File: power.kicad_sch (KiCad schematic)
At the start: 37 parts, among them J2 USB_C_Receptacle_USB2.0, Q1 AO3401A, Q2 AO3400A, SW1 SW_SPDT, U2 XC6220B331MR, U3 TLV70237_SOT23-5, U4 LN4913, U5 SRV05-4

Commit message: routed
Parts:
- removed C1: 0.1uF, Capacitor_SMD:C_0603_1608Metric, symbol Device:C
- removed JP3: SolderJumper_3_Open, Jumper:SolderJumper-3_P1.3mm_Open_RoundedPad1.0x1.5mm, symbol Jumper:SolderJumper_3_Open
- removed Q1: AO3401A, Package_TO_SOT_SMD:SOT-23, symbol Transistor_FET:AO3401A
- removed Q2: AO3400A, Package_TO_SOT_SMD:SOT-23, symbol Transistor_FET:AO3400A
- removed R23: 10M, Resistor_SMD:R_0603_1608Metric, symbol Device:R
- removed R9: 1M, Resistor_SMD:R_0603_1608Metric, symbol Device:R
- removed SC?: Solar_Cell, misc:KXOB25-05X3F, symbol Device:Solar_Cell
- removed SW1: SW_SPDT, Button_Switch_SMD:SW_SPDT_PCM12, symbol Switch:SW_SPDT
- removed U4: LN4913, Package_TO_SOT_SMD:SOT-23, symbol Sensor_Magnetic:A1101ELHL
- gave numbers to parts that had none: 19
- renumbered D1 to D3, R8 to R10, R3 to R11, R5 to R12, R7 to R9, U2 to U4, U3 to U5, U5 to U6
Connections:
- net 3V3_EN is gone; now on net SOLAR_OUT: U4.3 (CE)
- net D+: now also U6.1 (IO1), U6.6 (IO4); no longer U6.3 (IO2), U6.4 (IO3)
- net D-: now also U6.3 (IO2), U6.4 (IO3); no longer U6.1 (IO1), U6.6 (IO4)

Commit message: no screen
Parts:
- removed JP3: ~, Jumper:SolderJumper-2_P1.3mm_Open_RoundedPad1.0x1.5mm, symbol Jumper:SolderJumper_2_Open
- removed JP4: SolderJumper_2_Open, Jumper:SolderJumper-2_P1.3mm_Open_RoundedPad1.0x1.5mm, symbol Jumper:SolderJumper_2_Open
- added R7: 1M, Resistor_SMD:R_0603_1608Metric, symbol Device:R_Small
- C4: footprint Capacitor_THT:CP_Radial_D13.0mm_P5.00mm -> Capacitor_THT:CP_Radial_D16.0mm_P7.50mm
- C8: value 47uF -> 4.7uF
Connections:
- net SOLAR_OUT: now also R7.2; no longer U4.3 (CE)
- net at U7.11 (VBAT_OK): now also U4.3 (CE), R7.1
- no-connect marks 4 -> 3
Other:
- moved on the sheet: U4

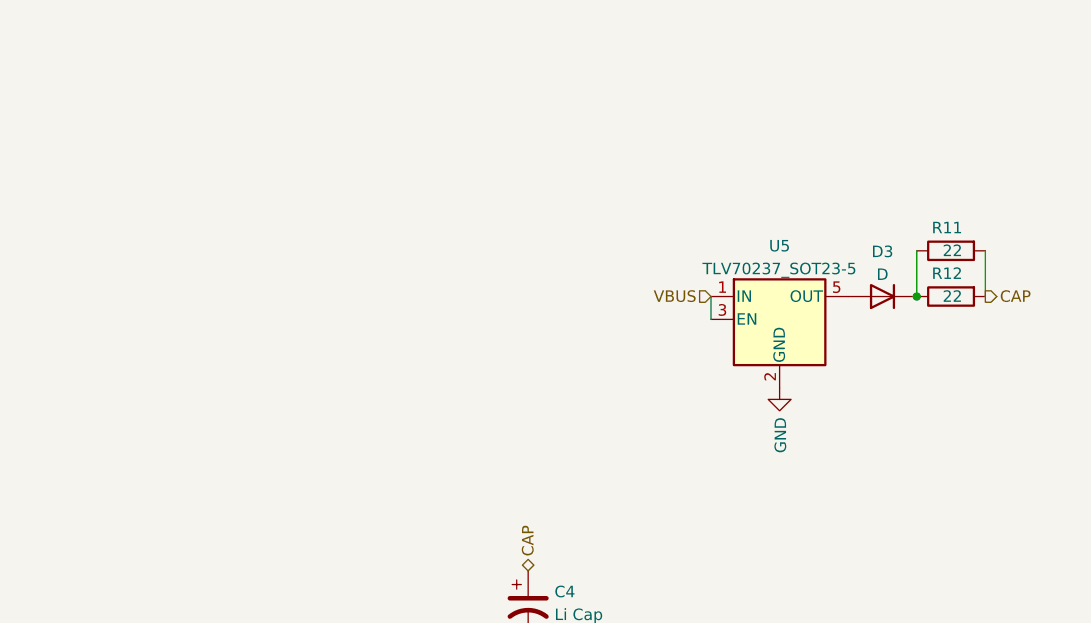
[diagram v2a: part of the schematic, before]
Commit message: scroll wheel + constant current charger
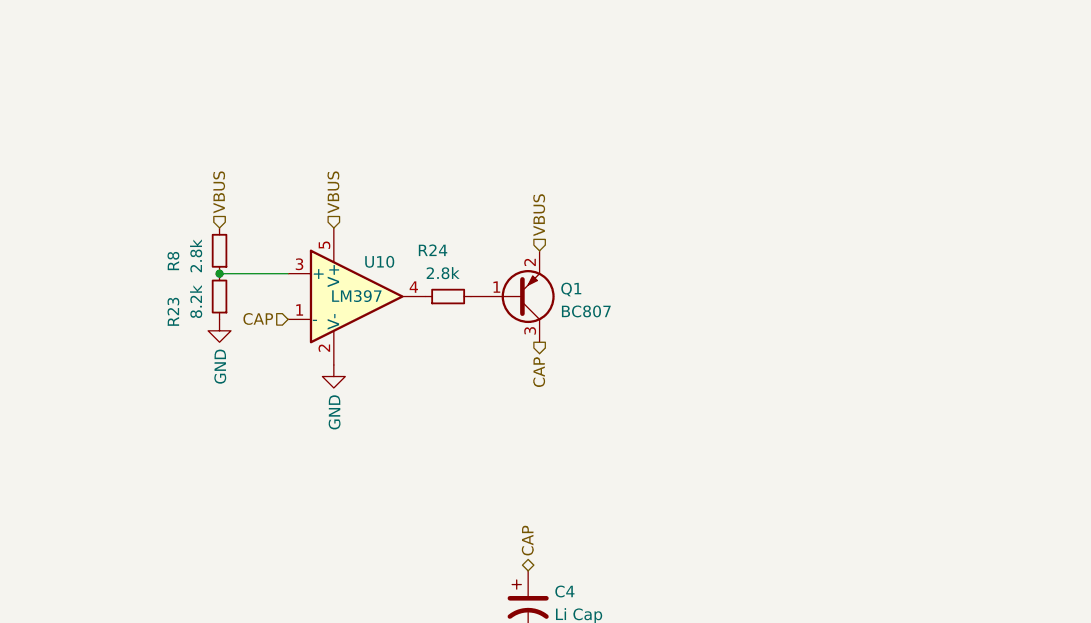
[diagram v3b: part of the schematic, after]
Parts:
- removed D3: D, Diode_SMD:D_SOD-123, symbol Device:D
- removed R11, R12: 22, Resistor_SMD:R_0603_1608Metric, symbol Device:R
- removed U5: TLV70237_SOT23-5, Package_TO_SOT_SMD:SOT-23-5, symbol Regulator_Linear:TLV70237_SOT23-5
- added Q1: BC807, Package_TO_SOT_SMD:SOT-23, symbol Transistor_BJT:BC807
- added R23: 8.2k, Resistor_SMD:R_0603_1608Metric, symbol Device:R_Small
- added R24, R8: 2.8k, Resistor_SMD:R_0603_1608Metric, symbol Device:R_Small
- added U10: LM397, Package_TO_SOT_SMD:SOT-23-5, symbol Comparator:LM397
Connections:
- net CAP: now also Q1.3 (C), U10.1 (-)
- net GND: now also R23.1, U10.2 (V-)
- net VBUS: now also Q1.2 (E), R8.2, U10.5 (V+)
- new net: R23.2, R8.1, U10.3 (+)
- new net: R24.1, U10.4
- new net: Q1.1 (B), R24.2

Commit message: done
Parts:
- added BT1: li-ion, Connector_JST:JST_PH_S2B-PH-SM4-TB_1x02-1MP_P2.00mm_Horizontal, symbol Device:Battery_Cell
- added C16: 1u, Capacitor_SMD:C_0603_1608Metric, symbol Device:C
- R24: value 2.8k -> ?
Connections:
- net 3V3: now also C16.1
- net CAP: now also BT1.1 (+)
- net GND: now also BT1.2 (-), C16.2
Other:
- moved on the sheet: C4, J2, Q1, R10, R23, R24, R8, R9, U10, U6

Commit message: swap bms and reg
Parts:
- removed C4: Li Cap, Capacitor_THT:CP_Radial_D16.0mm_P7.50mm, symbol Device:C_Polarized_US
- removed C6: 10nF, Capacitor_SMD:C_0603_1608Metric, symbol Device:C_Small
- removed C8: 4.7uF, Capacitor_SMD:C_0805_2012Metric, symbol Device:C
- removed Q1: BC807, Package_TO_SOT_SMD:SOT-23, symbol Transistor_BJT:BC807
- removed R13, R21: 4.12M, Resistor_SMD:R_0603_1608Metric, symbol Device:R_Small
- removed R14: 10M, Resistor_SMD:R_0603_1608Metric, symbol Device:R_Small
- removed R15: 5.9M, Resistor_SMD:R_0603_1608Metric, symbol Device:R_Small
- removed R16, R17, R18, R19: 5.1M, Resistor_SMD:R_0603_1608Metric, symbol Device:R_Small
- removed R20, R7: 1M, Resistor_SMD:R_0603_1608Metric, symbol Device:R_Small
- removed R22: 4.87M, Resistor_SMD:R_0603_1608Metric, symbol Device:R_Small
- removed R23: 8.2k, Resistor_SMD:R_0603_1608Metric, symbol Device:R_Small
- removed R24: ?, Resistor_SMD:R_0603_1608Metric, symbol Device:R_Small
- removed R8: 2.8k, Resistor_SMD:R_0603_1608Metric, symbol Device:R_Small
- removed U10: LM397, Package_TO_SOT_SMD:SOT-23-5, symbol Comparator:LM397
- removed U7: ~, Package_DFN_QFN:QFN-16-1EP_3x3mm_P0.5mm_EP1.7x1.7mm, symbol Battery_Management:BQ25504
- added C4, C6: 4.7uF, Capacitor_SMD:C_0603_1608Metric, symbol Device:C
- added R12, R13, R14: 100k, Resistor_SMD:R_0603_1608Metric, symbol Device:R
- added R7, R8: 10k, Resistor_SMD:R_0603_1608Metric, symbol Device:R
- added U5: BQ24072, Package_DFN_QFN:VQFN-16-1EP_3x3mm_P0.5mm_EP1.68x1.68mm_ThermalVias, symbol Battery_Management:BQ24075
- added U7: TLV62568DBV, Package_TO_SOT_SMD:SOT-23-5, symbol Regulator_Switching:TLV62568DBV
- C7: value 0.1uF -> 10uF
- L2: value 22uH -> 2.2uH; footprint Inductor_SMD:L_Wuerth_WE-TPC-3816 -> Inductor_SMD:L_1008_2520Metric; lcsc-part (none) -> C354533
- U4: lcsc-part (none) -> C5446
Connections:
- net GND: now also C4.2, C6.2, R14.1, R7.2, R8.2, U5.15 (SYSOFF), U5.17 (PAD), U5.4 (~{CE}), U5.5 (EN2), U5.8 (VSS), U7.2 (GND)
- net VBUS: now also C4.1, U5.13 (IN)
- net VDDH: now reaches U4.3 (CE)
- net VDDH: now also C5.2, U4.1 (VIN), U5.10 (OUT), U5.11 (OUT), U5.6 (EN1), U7.1 (EN), U7.4 (VIN)
- net 1V8: now reaches L2.2
- net 1V8: now also C7.2, R12.1
- net CAP renamed BAT
- net BAT: now also C6.1, U5.2 (BAT), U5.3 (BAT)
- net SOLAR: no longer names the net of L2.1
- net SOLAR: now also U7.3 (SW); no longer C5.2
- removed net SOLAR_OUT: C7.2, U4.1 (VIN)
- new net: R12.2, R13.1
- new net: R13.2, R14.2, U7.5 (FB)
- new net: R7.1, U5.1 (TS)
- new net: R8.1, U5.16 (ISET)
- new net ~{CHG}: U5.9 (~{CHG})
- no-connect marks 3 -> 6
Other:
- moved on the sheet: C16, U4
